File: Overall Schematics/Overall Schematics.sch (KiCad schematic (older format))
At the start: 13 parts, among them U1 Teensy4.1

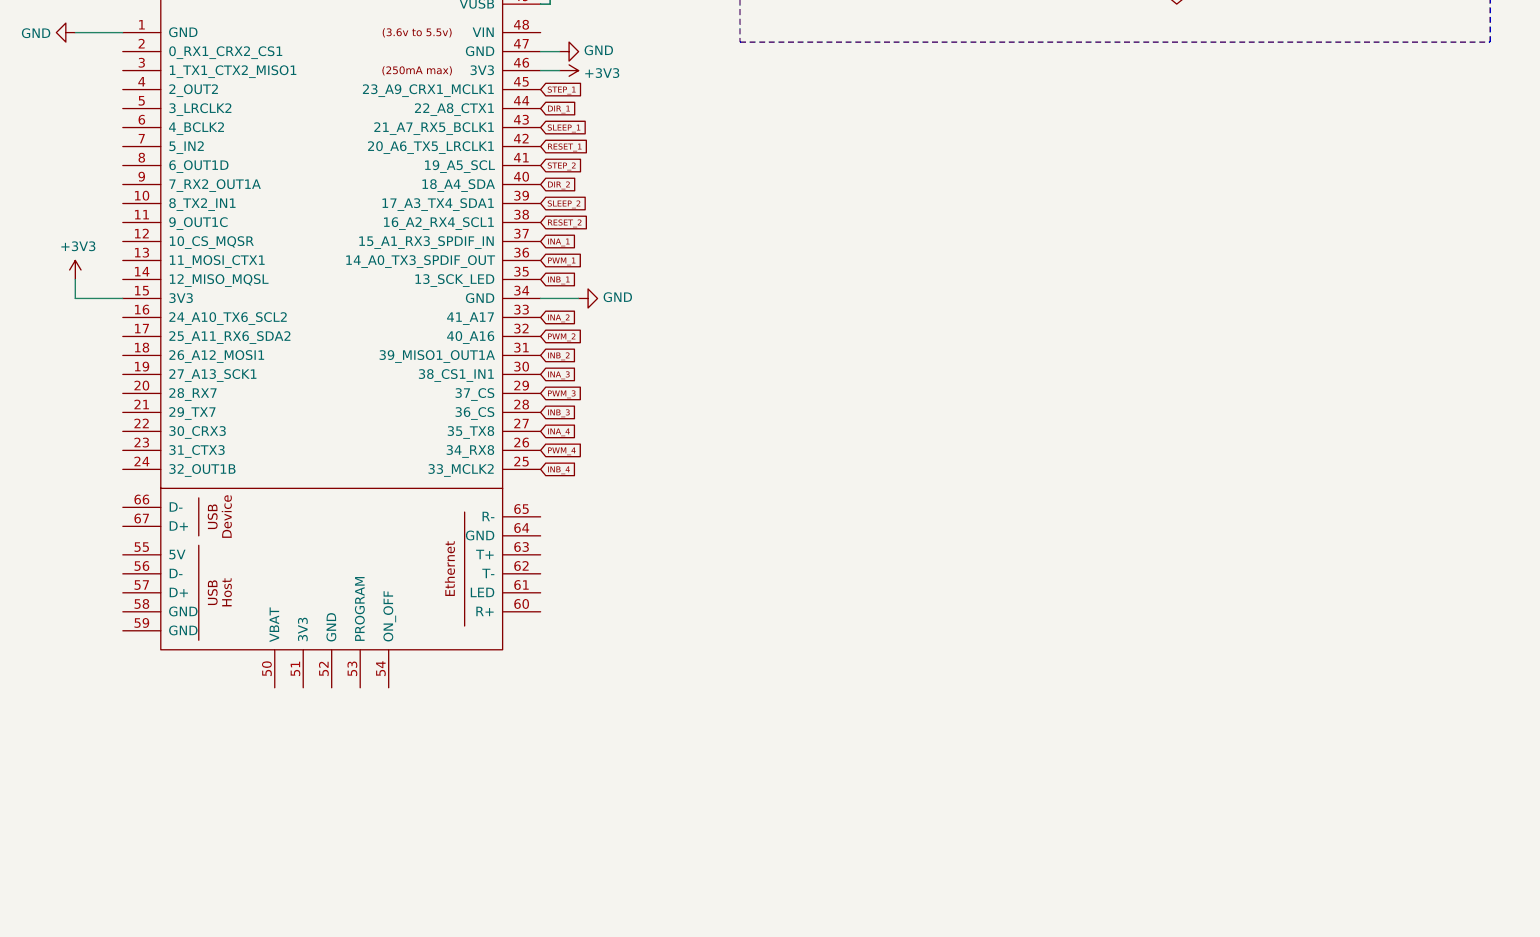
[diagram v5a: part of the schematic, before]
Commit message: Added Linear Actuators and DC Motor Controller
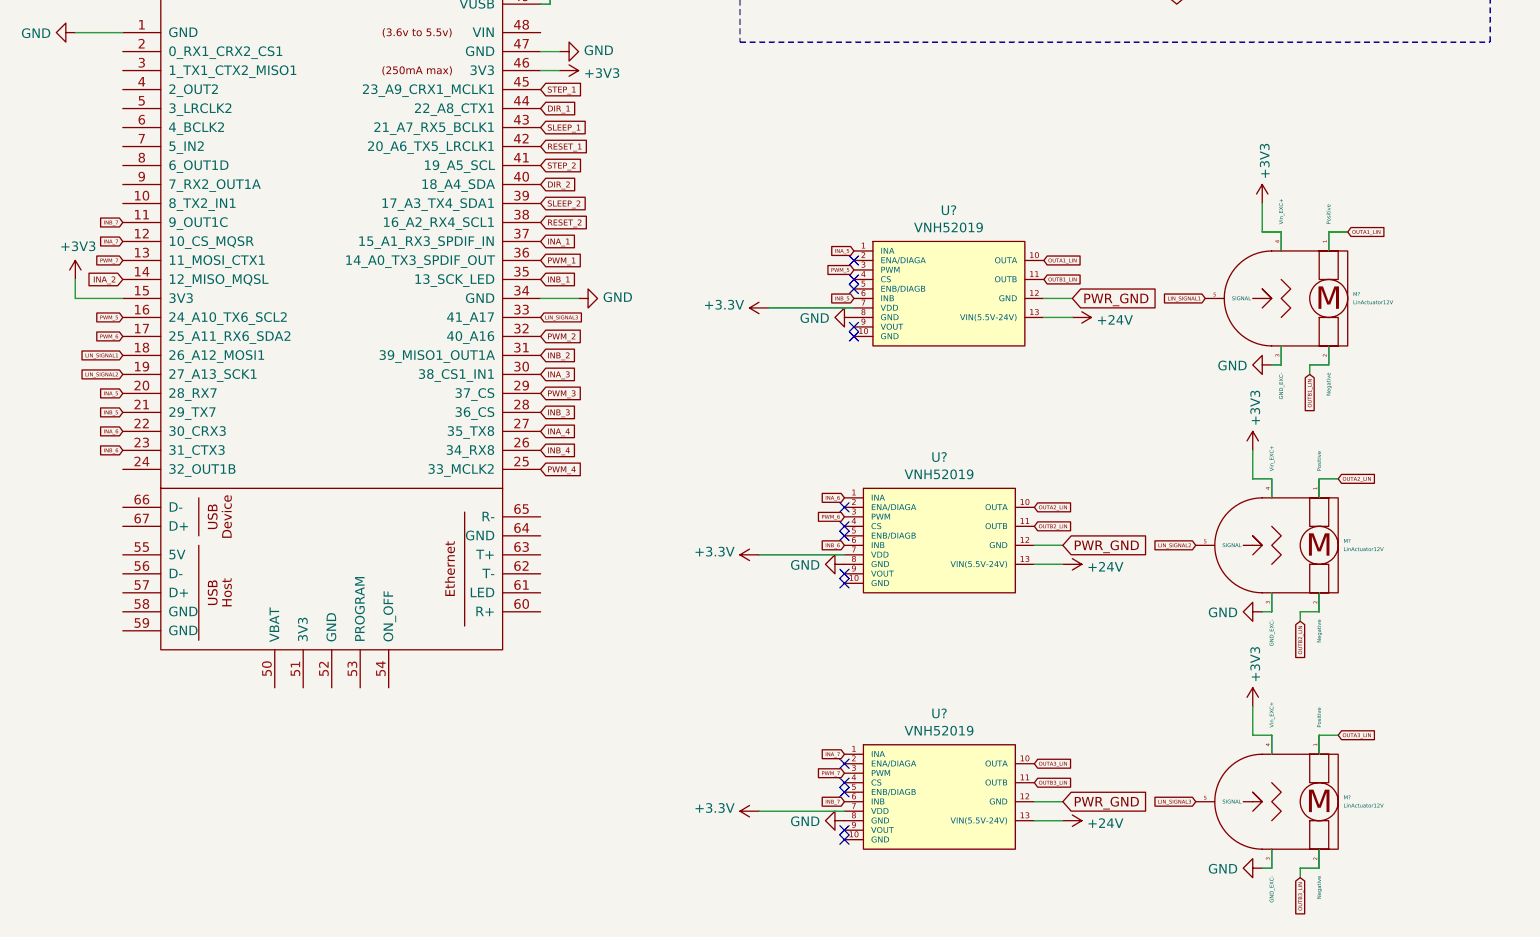
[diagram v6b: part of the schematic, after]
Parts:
- added M? (x3): LinActuator12V, symbol CustomLibrary:LinActuator12V
- added U? (x3): VNH52019, symbol CustomLibrary:VNH52019
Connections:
- net +24V: now also U?.13 (VIN(5.5V-24V)), U?.13 (VIN(5.5V-24V)), U?.13 (VIN(5.5V-24V))
- net +3V3: now also M?.4 (Vin_EXC+), M?.4 (Vin_EXC+), M?.4 (Vin_EXC+), U?.7 (VDD), U?.7 (VDD), U?.7 (VDD)
- net GND: now also M?.3 (GND_EXC-), M?.3 (GND_EXC-), M?.3 (GND_EXC-), U?.8 (GND), U?.8 (GND), U?.8 (GND)
- net INA_2: now also U1.14 (12_MISO_MQSL); no longer U1.33 (41_A17)
- net INB_4: now also U1.26 (34_RX8); no longer U1.25 (33_MCLK2)
- net PWM_4: now also U1.25 (33_MCLK2); no longer U1.26 (34_RX8)
- net PWR_GND: now also U?.12 (GND), U?.12 (GND), U?.12 (GND)
- net INB_7: now reaches U1.11 (9_OUT1C)
- net INB_7: now also U?.6 (INB)
- net INA_7: now reaches U1.12 (10_CS_MQSR)
- net INA_7: now also U?.1 (INA)
- net PWM_7: now reaches U1.13 (11_MOSI_CTX1)
- net PWM_7: now also U?.3 (PWM)
- net PWM_5: now reaches U1.16 (24_A10_TX6_SCL2)
- net PWM_5: now also U?.3 (PWM)
- net PWM_6: now reaches U1.17 (25_A11_RX6_SDA2)
- net PWM_6: now also U?.3 (PWM)
- net LIN_SIGNAL1: now reaches U1.18 (26_A12_MOSI1)
- net LIN_SIGNAL1: now also M?.5 (SIGNAL)
- net LIN_SIGNAL2: now reaches U1.19 (27_A13_SCK1)
- net LIN_SIGNAL2: now also M?.5 (SIGNAL)
- net INA_5: now reaches U1.20 (28_RX7)
- net INA_5: now also U?.1 (INA)
- net INB_5: now reaches U1.21 (29_TX7)
- net INB_5: now also U?.6 (INB)
- net INA_6: now reaches U1.22 (30_CRX3)
- net INA_6: now also U?.1 (INA)
- net INB_6: now reaches U1.23 (31_CTX3)
- net INB_6: now also U?.6 (INB)
- new net LIN_SIGNAL3: M?.5 (SIGNAL), U1.33 (41_A17)
- new net OUTA1_LIN: M?.1 (Positive), U?.10 (OUTA)
- new net OUTA2_LIN: M?.1 (Positive), U?.10 (OUTA)
- new net OUTA3_LIN: M?.1 (Positive), U?.10 (OUTA)
- new net OUTB1_LIN: M?.2 (Negative), U?.11 (OUTB)
- new net OUTB2_LIN: M?.2 (Negative), U?.11 (OUTB)
- new net OUTB3_LIN: M?.2 (Negative), U?.11 (OUTB)
- no-connect marks 42 -> 57

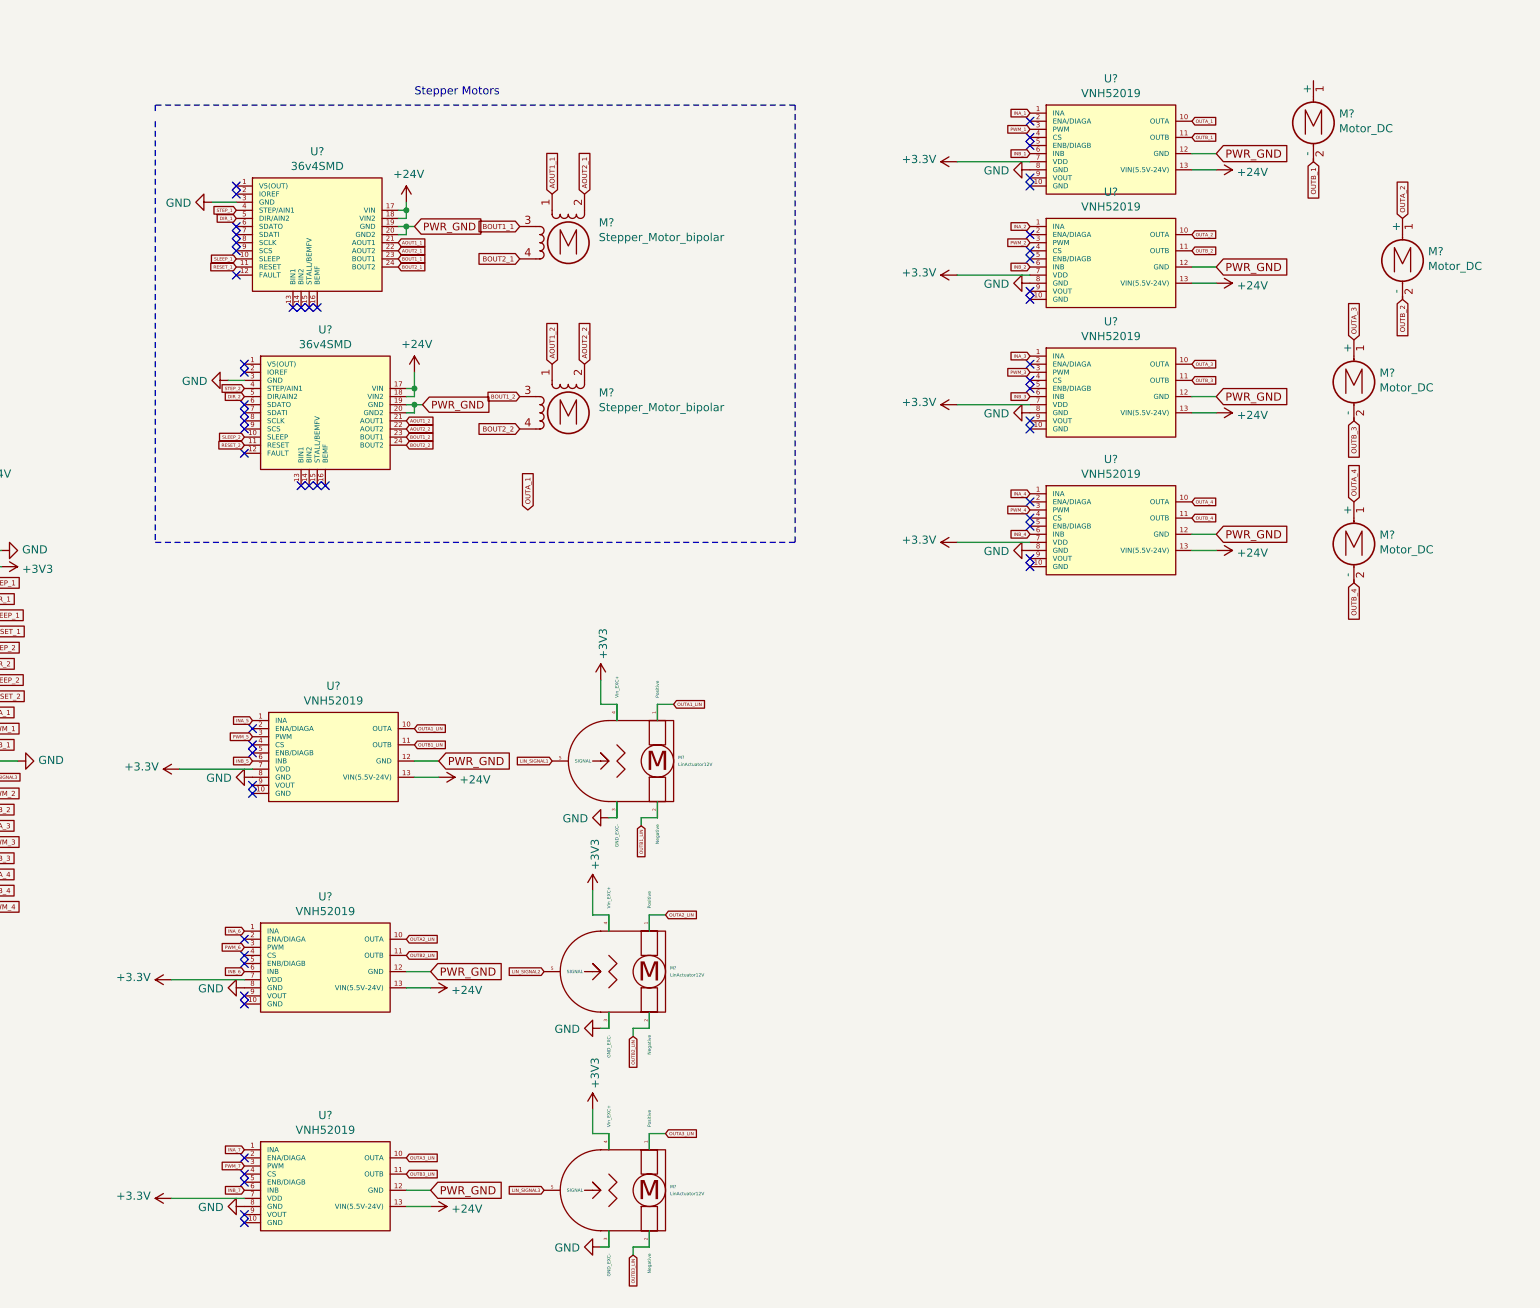
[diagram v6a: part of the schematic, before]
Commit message: Battery Changes
Added battery terminals, watt meter, and intel buck converter
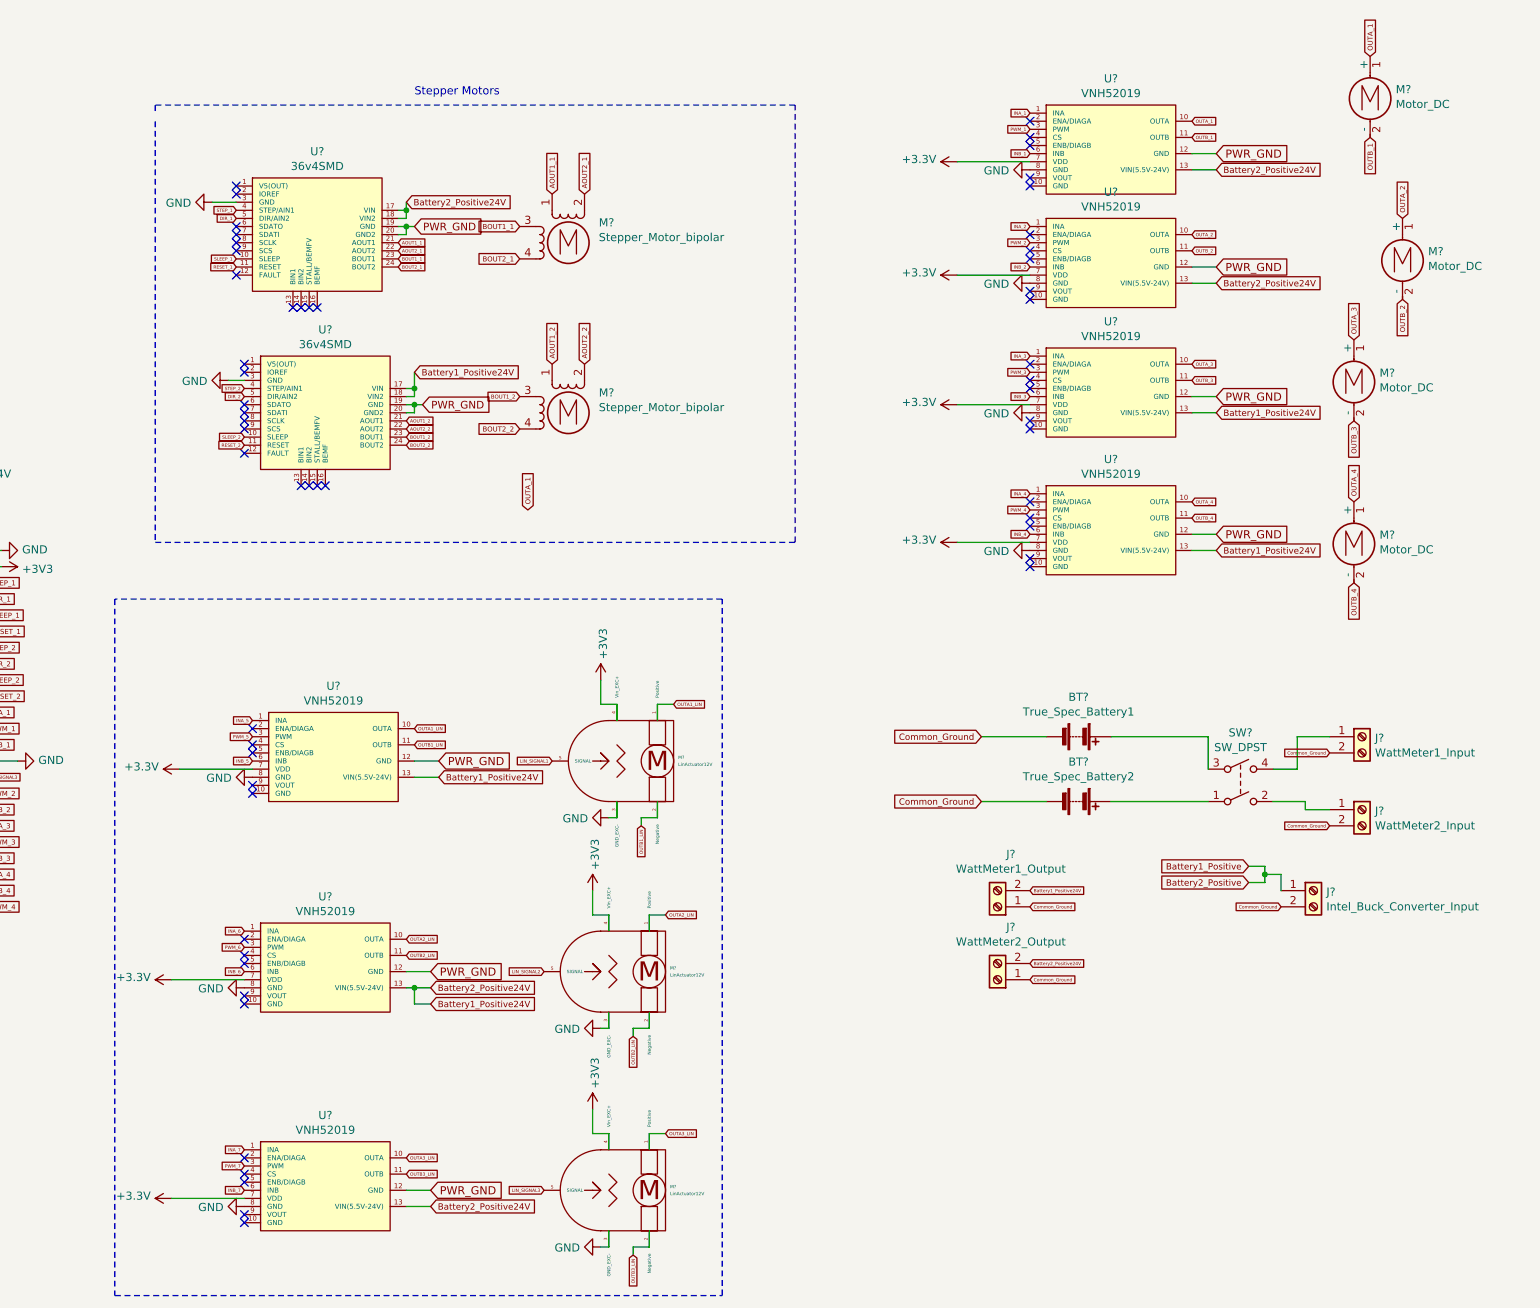
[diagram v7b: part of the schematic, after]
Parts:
- added BT?: True_Spec_Battery1, Custom Footprints:AMASS_XT60-M_1x02_P7.20mm_Vertical, symbol Device:Battery
- added BT?: True_Spec_Battery2, Custom Footprints:AMASS_XT60-M_1x02_P7.20mm_Vertical, symbol Device:Battery
- added J?: WattMeter1_Input, symbol Connector:Screw_Terminal_01x02
- added J?: WattMeter2_Input, symbol Connector:Screw_Terminal_01x02
- added J?: WattMeter1_Output, symbol Connector:Screw_Terminal_01x02
- added J?: WattMeter2_Output, symbol Connector:Screw_Terminal_01x02
- added J?: Intel_Buck_Converter_Input, symbol Connector:Screw_Terminal_01x02
- added SW?: SW_DPST, symbol Switch:SW_DPST
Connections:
- net +24V: no longer U?.13 (VIN(5.5V-24V)), U?.13 (VIN(5.5V-24V)), U?.13 (VIN(5.5V-24V)), U?.13 (VIN(5.5V-24V)), U?.13 (VIN(5.5V-24V)), U?.13 (VIN(5.5V-24V)), U?.13 (VIN(5.5V-24V)), U?.17 (VIN), U?.17 (VIN), U?.18 (VIN2), U?.18 (VIN2)
- net OUTA_1: now also M?.1 (+)
- new net: BT?.1 (+), SW?.3
- new net: BT?.1 (+), SW?.1
- new net: J?.1 (Pin_1), SW?.2
- new net: J?.1 (Pin_1), SW?.4
- new net Battery1_Positive: J?.1 (Pin_1)
- new net Battery1_Positive24V: J?.2 (Pin_2), J?.2 (Pin_2), U?.13 (VIN(5.5V-24V)), U?.13 (VIN(5.5V-24V)), U?.13 (VIN(5.5V-24V)), U?.13 (VIN(5.5V-24V)), U?.13 (VIN(5.5V-24V)), U?.13 (VIN(5.5V-24V)), U?.13 (VIN(5.5V-24V)), U?.17 (VIN), U?.17 (VIN), U?.18 (VIN2), U?.18 (VIN2)
- new net Common_Ground: BT?.2 (-), BT?.2 (-), J?.1 (Pin_1), J?.1 (Pin_1), J?.2 (Pin_2), J?.2 (Pin_2), J?.2 (Pin_2)
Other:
- moved on the sheet: M?
